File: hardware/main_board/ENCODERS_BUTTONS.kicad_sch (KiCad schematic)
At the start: 5 parts, among them J10 2x5 Socket Pins, J2 Conn_01x05_Pin, J3 Conn_01x05_Pin

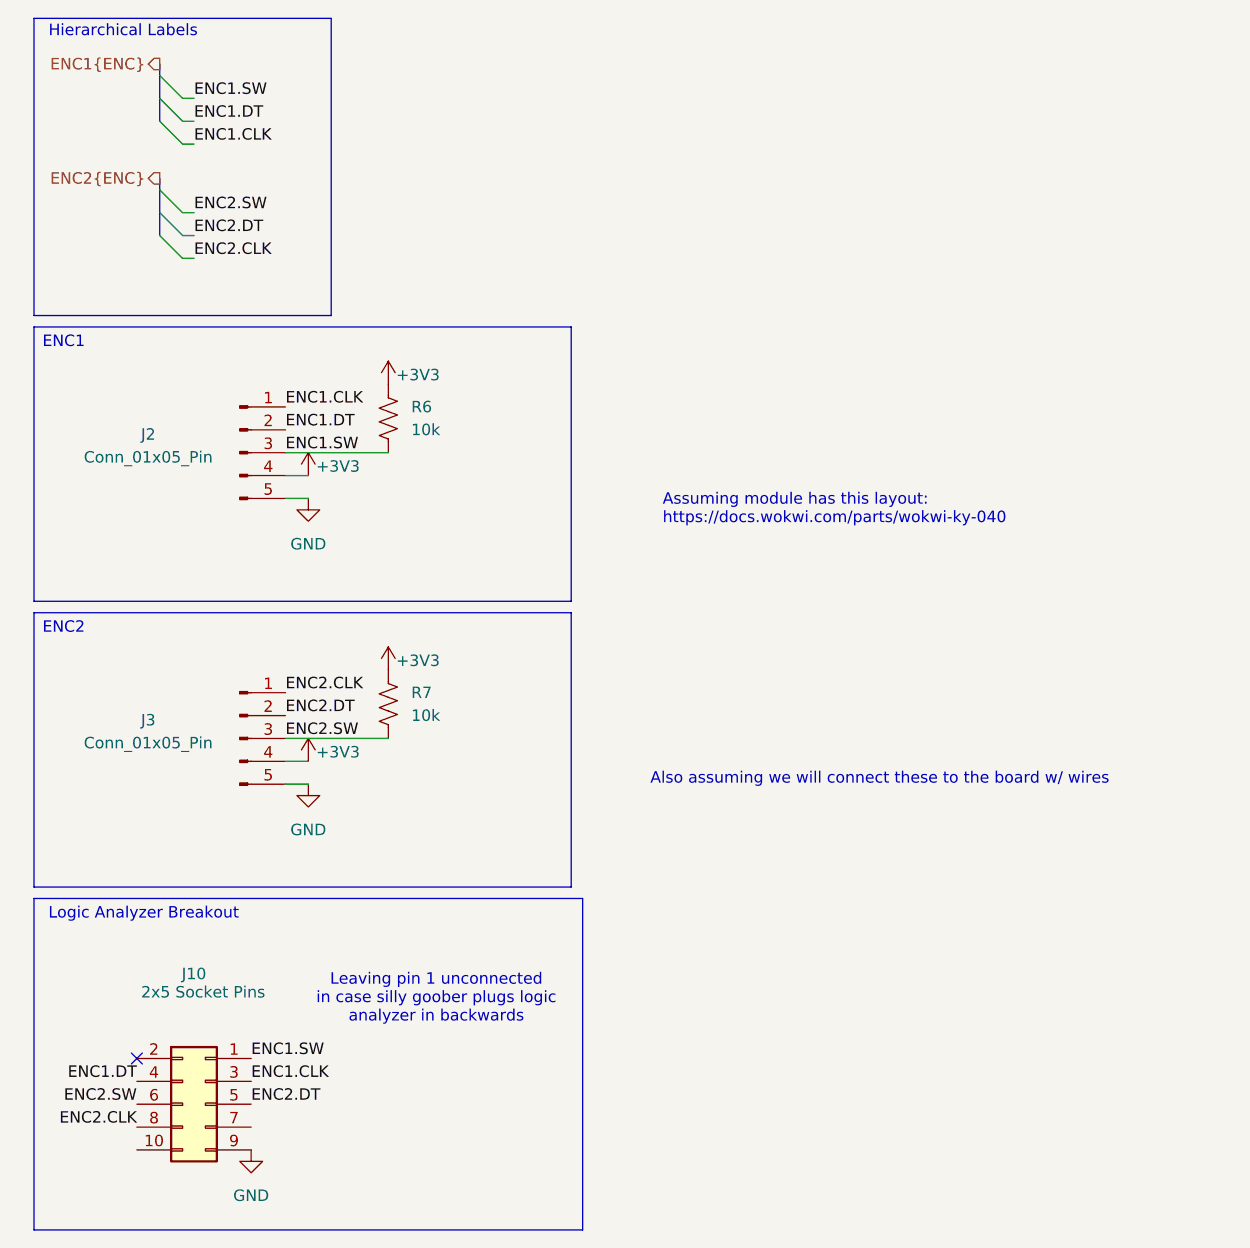
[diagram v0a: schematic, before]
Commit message: added lakshay suggestions to peripheral board. removed bypass jumper from main board audio amp. added led strip interface. added too many things to remember i forgor
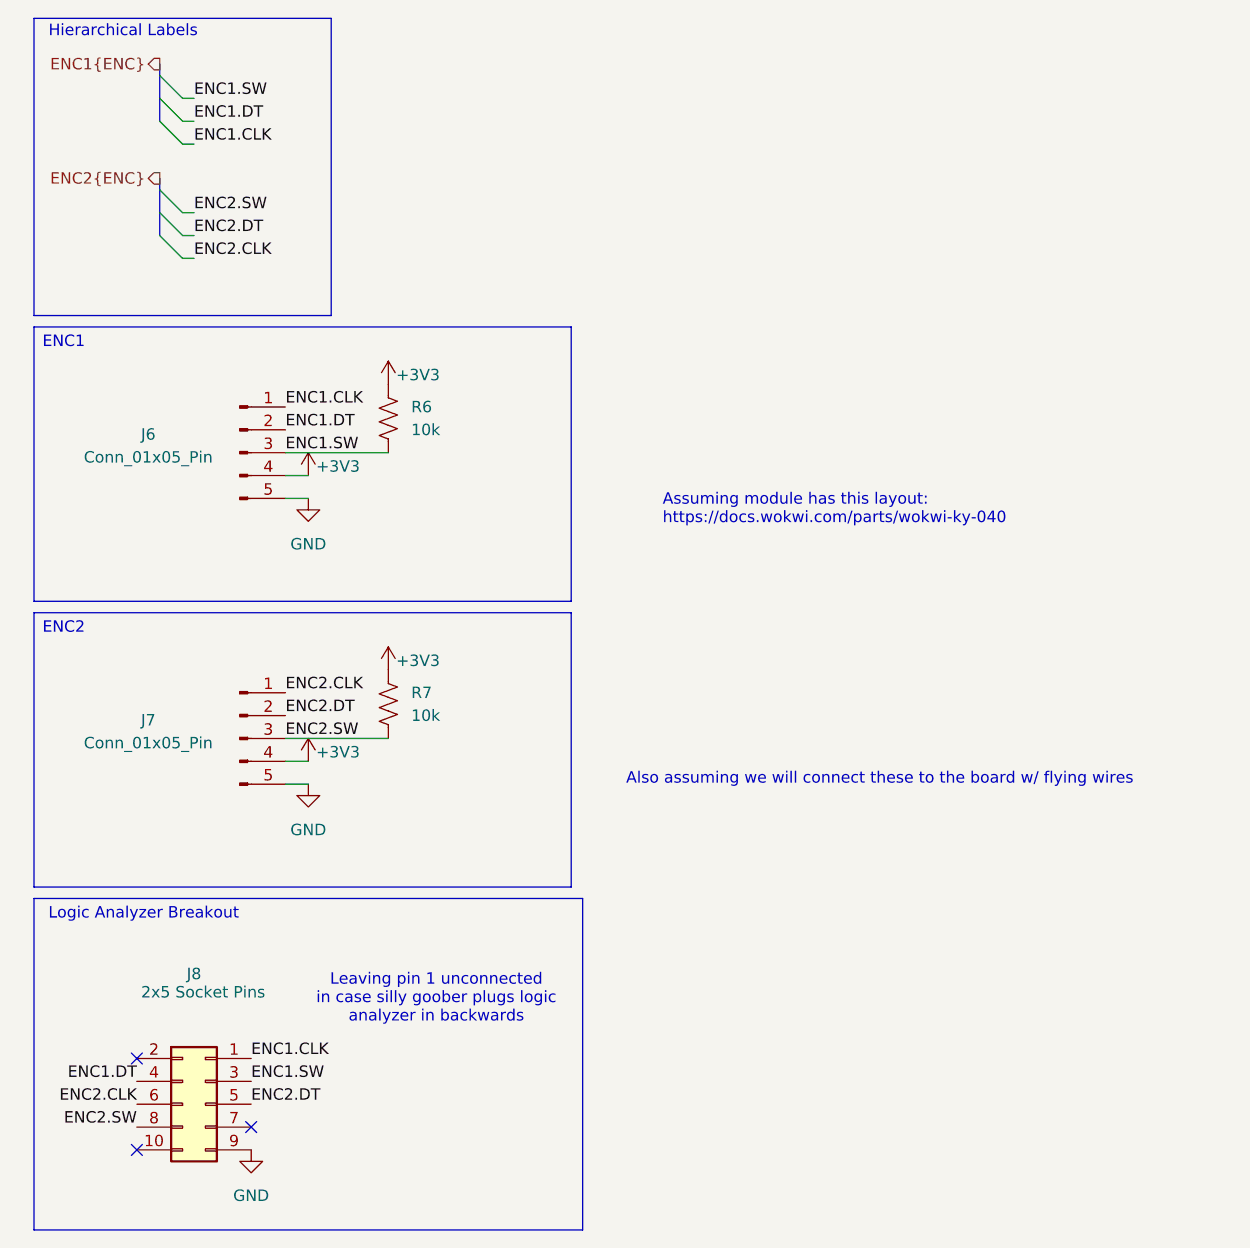
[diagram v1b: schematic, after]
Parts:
- renumbered J2 to J6, J3 to J7, J10 to J8
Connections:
- net ENC1.CLK: now also J8.1 (Pin_1); no longer J8.3 (Pin_3)
- net ENC1.SW: now also J8.3 (Pin_3); no longer J8.1 (Pin_1)
- net ENC2.CLK: now also J8.6 (Pin_6); no longer J8.8 (Pin_8)
- net ENC2.SW: now also J8.8 (Pin_8); no longer J8.6 (Pin_6)
- no-connect marks 1 -> 3
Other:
- note added: "Also assuming we will connect these to the board w/ flying wires"
- note removed: "Also assuming we will connect these to the board w/ wires"
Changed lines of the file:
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@@
 		)
 	)
-	(text "Also assuming we will connect these to the board w/ wires\n"
+	(text "Also assuming we will connect these to the board w/ flying wires\n"
 		(exclude_from_sim no)
 		(at 106.68 98.552 0)
@@
 			(justify left)
 		)
+	)
+	(no_connect
+		(at 24.13 139.7)
 	)
 	(no_connect
 		(at 24.13 129.54)
+	)
+	(no_connect
+		(at 36.83 137.16)
 	)
 	(bus_entry
@@
 	)
 	(label "ENC1.CLK"
-		(at 36.83 132.08 0)
+		(at 36.83 129.54 0)
 		(effects
 			(font
@@
 	)
 	(label "ENC2.SW"
+		(at 24.13 137.16 180)
+		(effects
+			(font
+				(size 1.27 1.27)
+			)
+			(justify right bottom)
+		)
+	)
+	(label "ENC2.CLK"
 		(at 24.13 134.62 180)
 		(effects
@@
 		)
 	)
-	(label "ENC2.CLK"
-		(at 24.13 137.16 180)
-		(effects
-			(font
-				(size 1.27 1.27)
-			)
-			(justify right bottom)
-		)
-	)
 	(label "ENC1.SW"
-		(at 36.83 129.54 0)
+		(at 36.83 132.08 0)
 		(effects
 			(font
@@
 		(on_board yes)
 		(dnp no)
-		(property "Reference" "#PWR020"
+		(property "Reference" "#PWR029"
 			(at 43.18 100.33 0)
 			(effects
@@
 			(project "main_board"
 				(path "/5332464e-0c3a-49d2-8fb5-731d0e42ee15/e8c3970d-4372-4a29-8ae6-7900eabb858b"
-					(reference "#PWR020")
+					(reference "#PWR029")
 					(unit 1)
 				)
@@
 		(on_board yes)
 		(dnp no)
-		(property "Reference" "#PWR019"
+		(property "Reference" "#PWR028"
 			(at 52.07 90.17 0)
 			(effects
@@
 			(project "main_board"
 				(path "/5332464e-0c3a-49d2-8fb5-731d0e42ee15/e8c3970d-4372-4a29-8ae6-7900eabb858b"
-					(reference "#PWR019")
+					(reference "#PWR028")
 					(unit 1)
 				)
@@
 		(on_board yes)
 		(dnp no)
-		(property "Reference" "J2"
+		(property "Reference" "J6"
 			(at 25.4 60.198 0)
 			(effects
@@
 			(project ""
 				(path "/5332464e-0c3a-49d2-8fb5-731d0e42ee15/e8c3970d-4372-4a29-8ae6-7900eabb858b"
-					(reference "J2")
+					(reference "J6")
 					(unit 1)
 				)
@@
 		(on_board yes)
 		(dnp no)
-		(property "Reference" "#PWR017"
+		(property "Reference" "#PWR026"
 			(at 43.18 68.58 0)
 			(effects
@@
 			(project ""
 				(path "/5332464e-0c3a-49d2-8fb5-731d0e42ee15/e8c3970d-4372-4a29-8ae6-7900eabb858b"
-					(reference "#PWR017")
+					(reference "#PWR026")
 					(unit 1)
 				)
@@
 		(dnp no)
 		(fields_autoplaced yes)
-		(property "Reference" "#PWR021"
+		(property "Reference" "#PWR030"
 			(at 43.18 105.41 0)
 			(effects
@@
 			(project "main_board"
 				(path "/5332464e-0c3a-49d2-8fb5-731d0e42ee15/e8c3970d-4372-4a29-8ae6-7900eabb858b"
-					(reference "#PWR021")
+					(reference "#PWR030")
 					(unit 1)
 				)
@@
 		(dnp no)
 		(fields_autoplaced yes)
-		(property "Reference" "#PWR09"
+		(property "Reference" "#PWR031"
 			(at 36.83 146.05 0)
 			(effects
@@
 			(project "main_board"
 				(path "/5332464e-0c3a-49d2-8fb5-731d0e42ee15/e8c3970d-4372-4a29-8ae6-7900eabb858b"
-					(reference "#PWR09")
+					(reference "#PWR031")
 					(unit 1)
 				)
@@
 		(on_board yes)
 		(dnp no)
-		(property "Reference" "J10"
+		(property "Reference" "J8"
 			(at 30.48 120.142 0)
 			(effects
@@
 			(project "main_board"
 				(path "/5332464e-0c3a-49d2-8fb5-731d0e42ee15/e8c3970d-4372-4a29-8ae6-7900eabb858b"
-					(reference "J10")
+					(reference "J8")
 					(unit 1)
 				)
@@
 		(on_board yes)
 		(dnp no)
-		(property "Reference" "#PWR016"
+		(property "Reference" "#PWR025"
 			(at 52.07 58.42 0)
 			(effects
@@
 			(project "main_board"
 				(path "/5332464e-0c3a-49d2-8fb5-731d0e42ee15/e8c3970d-4372-4a29-8ae6-7900eabb858b"
-					(reference "#PWR016")
+					(reference "#PWR025")
 					(unit 1)
 				)
@@
 		(dnp no)
 		(fields_autoplaced yes)
-		(property "Reference" "#PWR018"
+		(property "Reference" "#PWR027"
 			(at 43.18 73.66 0)
 			(effects
@@
 			(project ""
 				(path "/5332464e-0c3a-49d2-8fb5-731d0e42ee15/e8c3970d-4372-4a29-8ae6-7900eabb858b"
-					(reference "#PWR018")
+					(reference "#PWR027")
 					(unit 1)
 				)
@@
 		(on_board yes)
 		(dnp no)
-		(property "Reference" "J3"
+		(property "Reference" "J7"
 			(at 25.4 91.948 0)
 			(effects
@@
 			(project "main_board"
 				(path "/5332464e-0c3a-49d2-8fb5-731d0e42ee15/e8c3970d-4372-4a29-8ae6-7900eabb858b"
-					(reference "J3")
+					(reference "J7")
 					(unit 1)
 				)
